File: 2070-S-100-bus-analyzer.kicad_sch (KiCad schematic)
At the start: 88 parts, among them J10 Conn_02x13_Odd_Even, J11 Conn_02x13_Odd_Even, J12 USB4105-GF-A, J13 Conn_01x01, J14 Conn_01x01, J15 Conn_01x02, J16 Conn_01x02, J17 Conn_01x02, J18 Conn_01x02, J19 Conn_01x02, J2 Conn_02x13_Odd_Even, J3 Conn_02x13_Odd_Even, J4 Conn_02x13_Odd_Even, J5 Conn_02x13_Odd_Even, J6 Conn_02x13_Odd_Even, J7 Conn_02x13_Odd_Even, J8 Conn_02x13_Odd_Even, J9 Conn_02x13_Odd_Even, SW1 SW_MEC_5E, U1 74LVCH245APW,118, U10 74LVCH245APW,118, U11 74LVCH245APW,118, U12 74LVCH245APW,118, U13 74LVCH245APW,118, U14 74LVCH245APW,118, U15 74LVCH245APW,118, U16 AP63300, U17 LMS78_05-2.0R, U2 74LVCH245APW,118, U3 74LVCH245APW,118, U4 74LVCH245APW,118, U5 74LVCH245APW,118, U6 74LVCH245APW,118, U7 74LVCH245APW,118, U8 74LVCH245APW,118, U9 74LVCH245APW,118

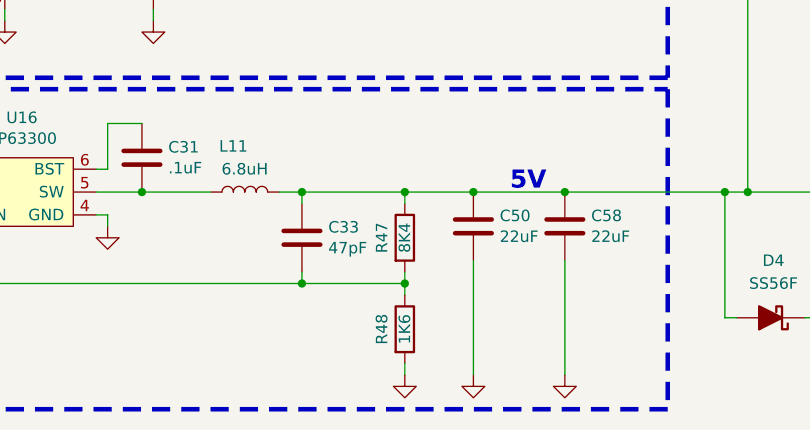
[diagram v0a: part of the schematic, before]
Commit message: update power supply as per wiggle
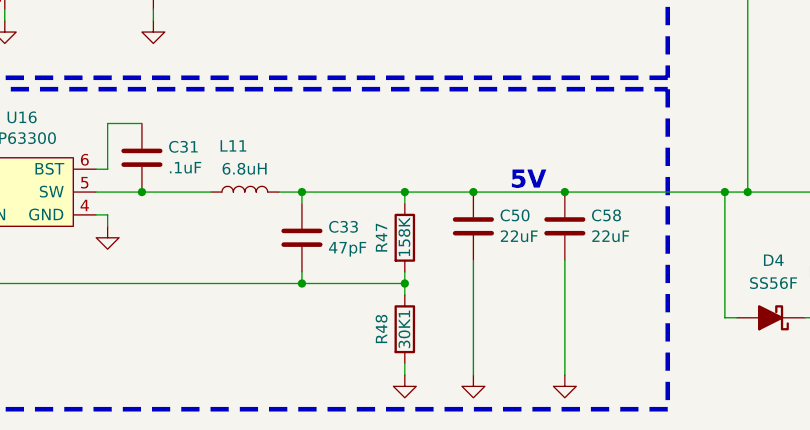
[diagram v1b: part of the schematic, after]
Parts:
- R47: value 8K4 -> 158K; Digi-Key_PN RMCF0603FT8K45CT-ND -> 13-RT0603FRE07158KLCT-ND; MPN RMCF0603FT8K45 -> RT0603FRE07158KL; Manufacturer Stackpole Electronics Inc -> YAGEO
- R48: value 1K6 -> 30K1; Digi-Key_PN RMCF0603FT1K60CT-ND -> 13-RT0603FRE0730K1LCT-ND; MPN RMCF0603FT1K60 -> RT0603FRE0730K1L; Manufacturer Stackpole Electronics Inc -> (none)
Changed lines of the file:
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@@
 			)
 		)
-		(property "Value" "8K4"
+		(property "Value" "158K"
 			(at 339.09 377.19 90)
 			(effects
@@
 			)
 		)
-		(property "Datasheet" ""
+		(property "Datasheet" "https://yageogroup.com/content/datasheet/asset/file/PYU-RT_1-TO-0-01_ROHS_L"
 			(at 339.09 377.19 0)
 			(effects
@@
 			)
 		)
-		(property "Description" "RES 8.45K OHM 1% 1/10W 0603"
+		(property "Description" "RES SMD 158K OHM 1% 1/10W 0603"
 			(at 339.09 377.19 0)
 			(effects
@@
 			)
 		)
-		(property "Digi-Key_PN" "RMCF0603FT8K45CT-ND"
+		(property "Digi-Key_PN" "13-RT0603FRE07158KLCT-ND"
 			(at 339.09 377.19 0)
 			(effects
@@
 			)
 		)
-		(property "MPN" "RMCF0603FT8K45"
+		(property "MPN" "RT0603FRE07158KL"
 			(at 339.09 377.19 0)
 			(effects
@@
 			)
 		)
-		(property "Manufacturer" "Stackpole Electronics Inc"
+		(property "Manufacturer" "YAGEO"
 			(at 339.09 377.19 0)
 			(effects
@@
 			)
 		)
-		(property "Value" "1K6"
+		(property "Value" "30K1"
 			(at 339.09 387.35 90)
 			(effects
@@
 			)
 		)
-		(property "Datasheet" ""
+		(property "Datasheet" "https://yageogroup.com/content/datasheet/asset/file/PYU-RT_1-TO-0-01_ROHS_L"
 			(at 339.09 387.35 0)
 			(effects
@@
 			)
 		)
-		(property "Description" "RES 1.6K OHM 1% 1/10W 0603"
+		(property "Description" "RES SMD 30.1K OHM 1% 1/10W 0603"
 			(at 339.09 387.35 0)
 			(effects
@@
 			)
 		)
-		(property "Digi-Key_PN" "RMCF0603FT1K60CT-ND"
+		(property "Digi-Key_PN" "13-RT0603FRE0730K1LCT-ND"
 			(at 339.09 387.35 0)
 			(effects
@@
 			)
 		)
-		(property "MPN" "RMCF0603FT1K60"
+		(property "MPN" "RT0603FRE0730K1L"
 			(at 339.09 387.35 0)
 			(effects
@@
 			)
 		)
-		(property "Manufacturer" "Stackpole Electronics Inc"
+		(property "Manufacturer" ""
 			(at 339.09 387.35 0)
 			(effects

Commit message: cosmetic stuff add gnd stiching vias
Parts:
- added TP1, TP2: TestPoint, TestPoint:TestPoint_Keystone_5015_Micro_Mini, symbol Connector:TestPoint
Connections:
- net GND: now also J5.23 (Pin_23), J9.23 (Pin_23), TP1.1, TP2.1
- no-connect marks 21 -> 19

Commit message: Remove OSHW from BOM
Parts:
- LOGO1: now left out of the parts list
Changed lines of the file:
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@@
 		(unit 1)
 		(exclude_from_sim no)
-		(in_bom yes)
+		(in_bom no)
 		(on_board yes)
 		(dnp no)

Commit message: BOM updates
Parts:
- A1, A2, A3, A4, A5: Digi-Key_PN (none) -> 2648-SC1631CT-ND; MPN (none) -> 2648-SC1631CT-ND; Manufacturer (none) -> Raspberry Pi
- C16, C66, C67: MPN (none) -> C2012X5R1V226M125AC; Manufacturer (none) -> TDK
- C33: Digi-Key_PN (none) -> 1276-1037-1-ND; MPN (none) -> CL10C470JB8NNNC; Manufacturer (none) -> Samsung Electro-Mechanics
- C47: value 10uF -> 10uF 25V; Digi-Key_PN (none) -> 587-2985-1-ND; MPN (none) -> TMK212BBJ106KG-T; Manufacturer (none) -> Taiyo Yuden
- D1, D2, D3: Digi-Key_PN (none) -> 475-LGR971-KN-1CT-ND; MPN (none) -> LG R971-KN-1-0-20-R18; Manufacturer (none) -> ams-OSRAM USA INC.
- D4, D5: MPN (none) -> SS56F; Manufacturer (none) -> Shenzhen Slkormicro Semicon Co., Ltd.
- H1, H2: MPN (none) -> CP-26 WE; Manufacturer (none) -> Bivar Inc.
- J1: value ~ -> S-100 Edge Connector
- J12: Digi-Key_PN (none) -> 2073-USB4105-GF-ACT-ND; MPN (none) -> USB4105-GF-A; Manufacturer (none) -> GCT
- R48: Manufacturer (none) -> YAGEO
- SW1: Digi-Key_PN (none) -> 450-1940-ND; MPN (none) -> 1-1825910-5; Manufacturer (none) -> TE Connectivity ALCOSWITCH Switches
- TP1, TP2: Digi-Key_PN (none) -> 2019-RCWCTECT-ND; MPN (none) -> RCWCTE; Manufacturer (none) -> KOA Speer Electronics, Inc.
- U1, U10, U11, U12, U13, U14, U15, U2, U3, U4, U5, U6, U7, U8, U9: MPN (none) -> 74LVCH245APW,118; Manufacturer (none) -> Nexperia USA Inc.
- U16: Digi-Key_PN 31-AP63300WU-7CT-ND -> 31-AP63301WU-7CT-ND; MPN AP63300WU-7 -> AP63301WU-7
- U17: MPN (none) -> LMS78_05-2.0RL; Manufacturer (none) -> GAPTEC Electronic

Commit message: Change trigger pulldown to 2.2K
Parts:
- R11: value 8K2 -> 2K2
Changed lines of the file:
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@@
 			)
 		)
-		(property "Value" "8K2"
+		(property "Value" "2K2"
 			(at 411.48 36.83 90)
 			(effects

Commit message: Rename /pDBIN as pDBIN & update silk
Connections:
- net ~{pDBIN} renamed pDBIN
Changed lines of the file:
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@@
 		)
 	)
-	(label "~{pDBIN}"
+	(label "pDBIN"
 		(at 327.66 228.6 0)
 		(effects
@@
 		)
 	)
-	(label "~{pDBIN}"
+	(label "pDBIN"
 		(at 229.87 101.6 180)
 		(effects

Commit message: Change /pSYNC to pSYNC & fix silk Larger testoints for gators
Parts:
- TP1, TP2: footprint TestPoint:TestPoint_Keystone_5015_Micro_Mini -> TestPoint:TestPoint_Keystone_5010-5014_Multipurpose; Digi-Key_PN 2019-RCWCTECT-ND -> (none); MPN RCWCTE -> (none); Manufacturer KOA Speer Electronics, Inc. -> (none)
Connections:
- net ~{pSYNC} renamed pSYNC
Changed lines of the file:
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@@
 		)
 	)
-	(label "~{pSYNC}"
+	(label "pSYNC"
 		(at 190.5 313.69 0)
 		(effects
@@
 		)
 	)
-	(label "~{pSYNC}"
+	(label "pSYNC"
 		(at 229.87 87.63 180)
 		(effects
@@
 			)
 		)
-		(property "Footprint" "TestPoint:TestPoint_Keystone_5015_Micro_Mini"
+		(property "Footprint" "TestPoint:TestPoint_Keystone_5010-5014_Multipurpose"
 			(at 298.45 49.53 0)
 			(effects
@@
 			)
 		)
-		(property "Datasheet" "https://www.koaspeer.com/pdfs/RC.pdf"
+		(property "Datasheet" ""
 			(at 298.45 49.53 0)
 			(effects
@@
 			)
 		)
-		(property "Description" "PC TEST POINT"
+		(property "Description" ""
 			(at 293.37 49.53 0)
 			(effects
@@
 			)
 		)
-		(property "Digi-Key_PN" "2019-RCWCTECT-ND"
+		(property "Digi-Key_PN" ""
 			(at 293.37 49.53 0)
 			(effects
@@
 			)
 		)
-		(property "MPN" "RCWCTE"
+		(property "MPN" ""
 			(at 293.37 49.53 0)
 			(effects
@@
 			)
 		)
-		(property "Manufacturer" "KOA Speer Electronics, Inc."
+		(property "Manufacturer" ""
 			(at 293.37 49.53 0)
 			(effects
@@
 			)
 		)
-		(property "Footprint" "TestPoint:TestPoint_Keystone_5015_Micro_Mini"
+		(property "Footprint" "TestPoint:TestPoint_Keystone_5010-5014_Multipurpose"
 			(at 280.67 49.53 0)
 			(effects
@@
 			)
 		)
-		(property "Datasheet" "https://www.koaspeer.com/pdfs/RC.pdf"
+		(property "Datasheet" ""
 			(at 280.67 49.53 0)
 			(effects
@@
 			)
 		)
-		(property "Description" "PC TEST POINT"
+		(property "Description" ""
 			(at 275.59 49.53 0)
 			(effects
@@
 			)
 		)
-		(property "Digi-Key_PN" "2019-RCWCTECT-ND"
+		(property "Digi-Key_PN" ""
 			(at 275.59 49.53 0)
 			(effects
@@
 			)
 		)
-		(property "MPN" "RCWCTE"
+		(property "MPN" ""
 			(at 275.59 49.53 0)
 			(effects
@@
 			)
 		)
-		(property "Manufacturer" "KOA Speer Electronics, Inc."
+		(property "Manufacturer" ""
 			(at 275.59 49.53 0)
 			(effects
